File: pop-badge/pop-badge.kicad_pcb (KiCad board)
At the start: 2 copper layers, 129.5 x 101.3 mm, 158 parts, among them J1 Conn_01x04, Q1 BC818, U1 WS2812-2020, U10 WS2812-2020, U11 WS2812-2020, U12 WS2812-2020, U13 WS2812-2020, U14 WS2812-2020, U15 WS2812-2020, U16 WS2812-2020, U17 WS2812-2020, U18 WS2812-2020, U19 WS2812-2020, U2 WS2812-2020, U20 WS2812-2020, U21 WS2812-2020, U22 WS2812-2020, U23 WS2812-2020, U24 WS2812-2020, U25 WS2812-2020, U26 Pico, U3 WS2812-2020, U4 WS2812-2020, U5 WS2812-2020, U6 WS2812-2020, U7 WS2812-2020, U8 WS2812-2020, U9 WS2812-2020

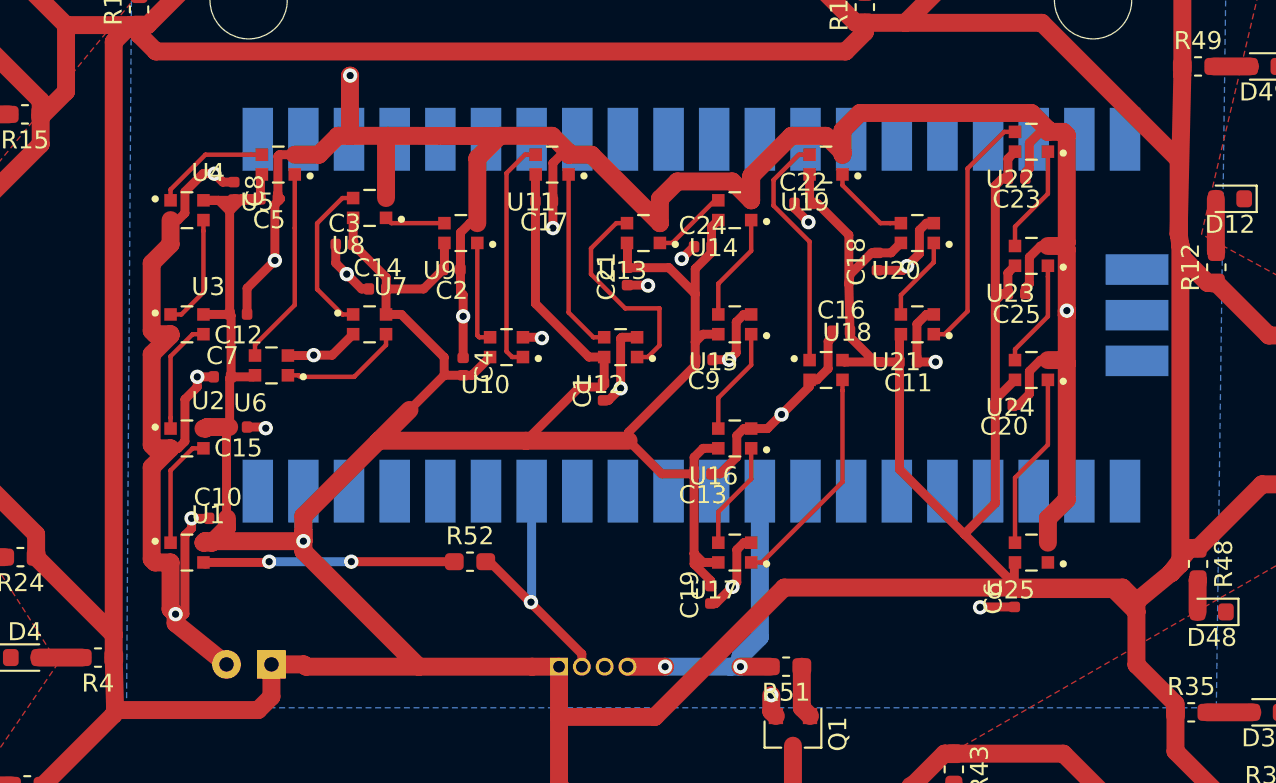
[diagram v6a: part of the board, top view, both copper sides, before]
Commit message: add a cut out for the usb connector
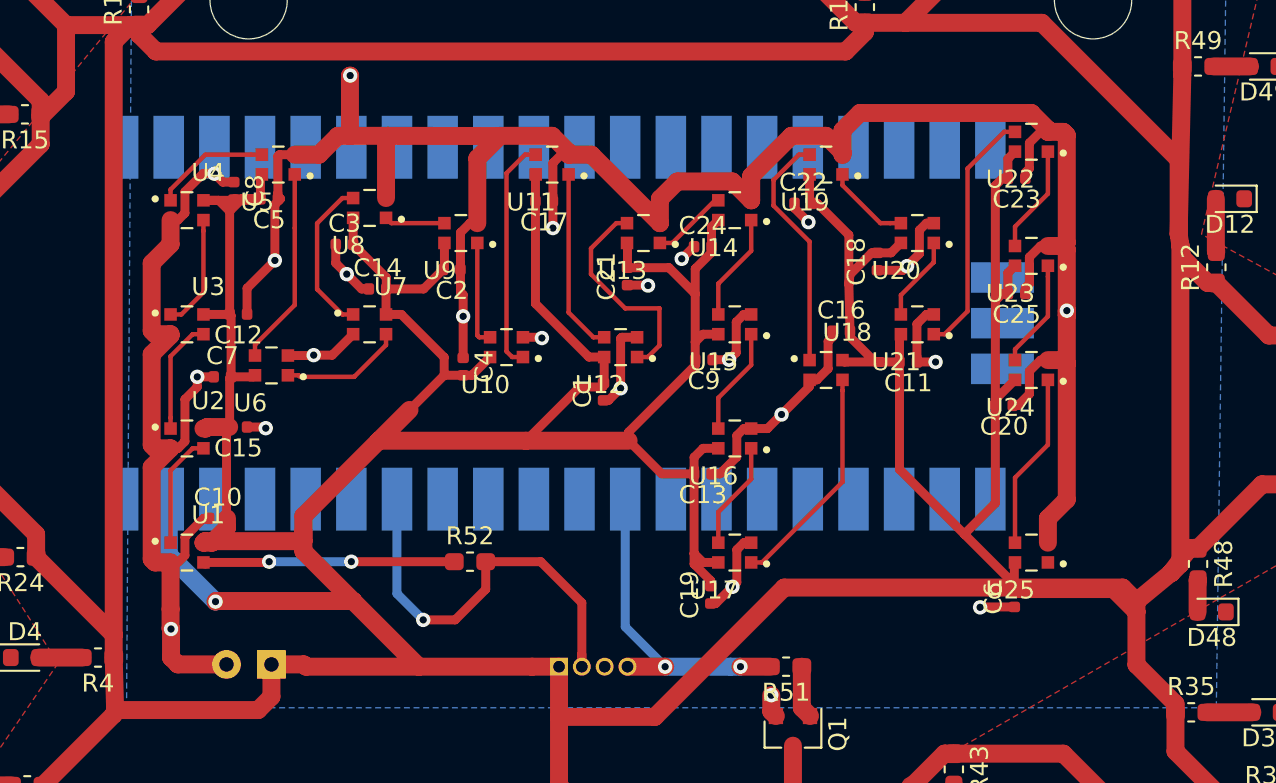
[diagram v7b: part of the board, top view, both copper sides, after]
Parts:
- moved U26 7.51 mm to (65.4, 90.4)
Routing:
- net +5V: track 824.7 -> 836.4 mm
- net DIN: track 15.4 -> 24.7 mm
- net GND: track 224.9 -> 222.9 mm, vias 24 -> 23
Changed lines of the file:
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@@
     (thickness 1.6)
     (drawings 17)
-    (tracks 730)
+    (tracks 738)
     (zones 0)
     (modules 158)
@@
   )
   (module RPi_Pico:RPi_Pico_SMD (layer B.Cu)
-    (at 72.898 89.916 270)
+    (at 65.405 90.3605 270)
     (descr "Through hole straight pin header, 2x20, 2.54mm pitch, double rows")
     (tags "Through hole pin header THT 2x20 2.54mm double row")
@@
   (segment (start 60.986 84.794) (end 60.986 81.1905) (width 1) (layer F.Cu) (net 32))
   (segment (start 62.23 79.9465) (end 56.019501 79.933999) (width 1) (layer F.Cu) (net 32))
-  (via (at 45.085 101.219) (size 0.8) (drill 0.4) (layers F.Cu B.Cu) (net 32))
-  (segment (start 46.0605 101.219) (end 45.085 101.219) (width 0.5) (layer F.Cu) (net 32))
   (via (at 49.2125 96.2025) (size 0.8) (drill 0.4) (layers F.Cu B.Cu) (net 32))
   (segment (start 49.149 96.139) (end 49.2125 96.2025) (width 0.5) (layer F.Cu) (net 32))
@@
   (segment (start 93.786001 92.603999) (end 93.786001 89.919499) (width 1) (layer F.Cu) (net 32))
   (segment (start 93.786001 89.919499) (end 93.786001 86.253999) (width 1) (layer F.Cu) (net 32))
-  (segment (start 43.916 106.273) (end 44.196 106.553) (width 1) (layer F.Cu) (net 32))
   (segment (start 43.916 103.674) (end 43.916 106.273) (width 1) (layer F.Cu) (net 32))
-  (via (at 44.196 106.553) (size 0.8) (drill 0.4) (layers F.Cu B.Cu) (net 32))
-  (segment (start 44.716001 106.540999) (end 44.196 107.061) (width 0.5) (layer F.Cu) (net 32))
-  (segment (start 45.085 101.784685) (end 44.716001 102.153684) (width 0.5) (layer F.Cu) (net 32))
-  (segment (start 44.716001 102.153684) (end 44.716001 106.540999) (width 0.5) (layer F.Cu) (net 32))
-  (segment (start 45.085 101.219) (end 45.085 101.784685) (width 0.5) (layer F.Cu) (net 32))
-  (segment (start 44.196 107.061) (end 47.03 109.347) (width 1) (layer F.Cu) (net 32))
-  (segment (start 44.196 106.553) (end 44.196 107.061) (width 1) (layer F.Cu) (net 32))
   (segment (start 44.332814 97.324) (end 43.916 97.324) (width 0.5) (layer F.Cu) (net 32))
   (segment (start 44.716001 96.940813) (end 44.332814 97.324) (width 0.5) (layer F.Cu) (net 32))
@@
   (segment (start 77.343 111.964) (end 77.5995 112.2205) (width 1) (layer F.Cu) (net 32))
   (segment (start 77.343 111.0615) (end 77.343 111.964) (width 1) (layer F.Cu) (net 32))
+  (segment (start 44.716001 103.284001) (end 44.326002 103.674) (width 0.5) (layer F.Cu) (net 32))
+  (segment (start 44.326002 103.674) (end 43.916 103.674) (width 0.5) (layer F.Cu) (net 32))
+  (segment (start 44.716001 102.260482) (end 44.716001 103.284001) (width 0.5) (layer F.Cu) (net 32))
+  (segment (start 45.757483 101.219) (end 44.716001 102.260482) (width 0.5) (layer F.Cu) (net 32))
+  (segment (start 46.0605 101.219) (end 45.757483 101.219) (width 0.5) (layer F.Cu) (net 32))
+  (via (at 43.942 107.3785) (size 0.8) (drill 0.4) (layers F.Cu B.Cu) (net 32))
+  (segment (start 43.916 106.273) (end 43.916 107.3525) (width 1) (layer F.Cu) (net 32))
+  (segment (start 43.942 107.3785) (end 43.916 107.3525) (width 1) (layer F.Cu) (net 32))
+  (segment (start 43.942 107.3785) (end 43.942 108.966) (width 1) (layer F.Cu) (net 32))
+  (segment (start 44.323 109.347) (end 47.03 109.347) (width 1) (layer F.Cu) (net 32))
+  (segment (start 43.942 108.966) (end 44.323 109.347) (width 1) (layer F.Cu) (net 32))
   (segment (start 61.667106 103.632) (end 61.454 103.632) (width 0.5) (layer F.Cu) (net 33))
   (segment (start 66.802 109.474) (end 66.802 108.766894) (width 0.5) (layer F.Cu) (net 33))
-  (segment (start 63.971947 105.881947) (end 64.008 105.918) (width 0.5) (layer F.Cu) (net 33))
-  (segment (start 63.917053 105.881947) (end 63.971947 105.881947) (width 0.5) (layer F.Cu) (net 33))
-  (segment (start 66.802 108.766894) (end 63.917053 105.881947) (width 0.5) (layer F.Cu) (net 33))
-  (segment (start 63.917053 105.881947) (end 61.667106 103.632) (width 0.5) (layer F.Cu) (net 33))
-  (segment (start 64.008 105.845894) (end 63.971947 105.881947) (width 0.5) (layer B.Cu) (net 33))
-  (via (at 63.971947 105.881947) (size 0.8) (drill 0.4) (layers F.Cu B.Cu) (net 33))
-  (segment (start 64.008 98.806) (end 64.008 105.845894) (width 0.5) (layer B.Cu) (net 33))
+  (via (at 57.9755 106.8705) (size 0.8) (drill 0.4) (layers F.Cu B.Cu) (net 33))
+  (segment (start 56.515 105.41) (end 57.9755 106.8705) (width 0.5) (layer B.Cu) (net 33))
+  (segment (start 56.515 99.2505) (end 56.515 105.41) (width 0.5) (layer B.Cu) (net 33))
+  (segment (start 57.9755 106.8705) (end 59.7535 106.8705) (width 0.5) (layer F.Cu) (net 33))
+  (segment (start 61.454 105.17) (end 61.454 103.632) (width 0.5) (layer F.Cu) (net 33))
+  (segment (start 59.7535 106.8705) (end 61.454 105.17) (width 0.5) (layer F.Cu) (net 33))
+  (segment (start 61.454 103.632) (end 64.516 103.632) (width 0.5) (layer F.Cu) (net 33))
+  (segment (start 66.802 105.918) (end 66.802 109.474) (width 0.5) (layer F.Cu) (net 33))
+  (segment (start 64.516 103.632) (end 66.802 105.918) (width 0.5) (layer F.Cu) (net 33))
   (segment (start 79.0495 109.48) (end 79.0435 109.474) (width 0.5) (layer F.Cu) (net 34))
   (segment (start 79.0435 111.7645) (end 79.4995 112.2205) (width 1) (layer F.Cu) (net 34))
@@
   (segment (start 92.736 97.129) (end 90.906 98.959) (width 0.25) (layer F.Cu) (net 78))
   (segment (start 65.532 116.092) (end 66.548 117.108) (width 1) (layer F.Cu) (net 80))
-  (via (at 51.308 102.489) (size 0.8) (drill 0.4) (layers F.Cu B.Cu) (net 80))
-  (segment (start 51.308 98.806) (end 51.308 102.489) (width 1) (layer B.Cu) (net 80))
   (segment (start 64.032 109.474) (end 65.532 109.474) (width 1) (layer F.Cu) (net 80))
   (segment (start 57.727315 109.474) (end 64.032 109.474) (width 1) (layer F.Cu) (net 80))
@@
   (segment (start 90.5105 81.2095) (end 90.5105 82.296) (width 0.5) (layer F.Cu) (net 80))
   (segment (start 90.906 80.814) (end 90.5105 81.2095) (width 0.5) (layer F.Cu) (net 80))
-  (segment (start 51.308 103.054685) (end 57.727315 109.474) (width 1) (layer F.Cu) (net 80))
   (segment (start 60.593 117.108) (end 60.579 117.094) (width 0.5) (layer F.Cu) (net 80))
   (segment (start 60.706 117.108) (end 60.593 117.108) (width 0.5) (layer F.Cu) (net 80))
@@
   (segment (start 41.689 73.773) (end 42.164 73.773) (width 1) (layer F.Cu) (net 80))
   (segment (start 40.753 74.709) (end 41.689 73.773) (width 1) (layer F.Cu) (net 80))
-  (segment (start 40.753 107.696) (end 40.753 74.709) (width 1) (layer F.Cu) (net 80))
   (segment (start 82.55 74.171) (end 82.55 73.646) (width 1) (layer F.Cu) (net 80))
   (segment (start 81.480999 75.240001) (end 82.55 74.171) (width 1) (layer F.Cu) (net 80))
@@
   (segment (start 65.532 112.268) (end 65.532 116.092) (width 1) (layer F.Cu) (net 80))
   (segment (start 65.532 109.474) (end 65.532 112.268) (width 1) (layer F.Cu) (net 80))
+  (segment (start 54.073158 105.825658) (end 54.102 105.8545) (width 1) (layer F.Cu) (net 80))
+  (segment (start 54.073158 105.819842) (end 54.073158 105.825658) (width 1) (layer F.Cu) (net 80))
+  (segment (start 51.308 103.054685) (end 54.073158 105.819842) (width 1) (layer F.Cu) (net 80))
+  (segment (start 54.073158 105.819842) (end 57.727315 109.474) (width 1) (layer F.Cu) (net 80))
+  (via (at 46.4185 105.8545) (size 0.8) (drill 0.4) (layers F.Cu B.Cu) (net 80))
+  (segment (start 46.453158 105.819842) (end 46.4185 105.8545) (width 1) (layer F.Cu) (net 80))
+  (segment (start 54.073158 105.819842) (end 46.453158 105.819842) (width 1) (layer F.Cu) (net 80))
+  (segment (start 43.815 103.251) (end 43.815 99.2505) (width 1) (layer B.Cu) (net 80))
+  (segment (start 46.4185 105.8545) (end 43.815 103.251) (width 1) (layer B.Cu) (net 80))
+  (segment (start 40.753 107.696) (end 40.753 74.709) (width 1) (layer F.Cu) (net 80))
   (via (at 75.6285 109.474) (size 0.8) (drill 0.4) (layers F.Cu B.Cu) (net 81))
   (segment (start 77.2935 109.474) (end 75.6285 109.474) (width 1) (layer F.Cu) (net 81))
@@
   (segment (start 75.062815 109.474) (end 71.4375 109.474) (width 1) (layer B.Cu) (net 81))
   (segment (start 71.4375 109.474) (end 69.342 109.474) (width 1) (layer F.Cu) (net 81))
-  (segment (start 76.708 107.828815) (end 76.708 98.806) (width 1) (layer B.Cu) (net 81))
-  (segment (start 75.6285 108.908315) (end 76.708 107.828815) (width 1) (layer B.Cu) (net 81))
-  (segment (start 75.6285 109.474) (end 75.6285 108.908315) (width 1) (layer B.Cu) (net 81))
+  (segment (start 69.215 107.2515) (end 71.4375 109.474) (width 0.5) (layer B.Cu) (net 81))
+  (segment (start 69.215 99.2505) (end 69.215 107.2515) (width 0.5) (layer B.Cu) (net 81))
   (segment (start 59.704 103.632) (end 59.69 103.632) (width 0.5) (layer F.Cu) (net 121))
   (via (at 53.975 103.632) (size 0.8) (drill 0.4) (layers F.Cu B.Cu) (net 121))
